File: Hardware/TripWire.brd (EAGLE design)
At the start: 27.3 x 45.2 mm, 40 parts, among them X1 GADGETEER-SOCKET

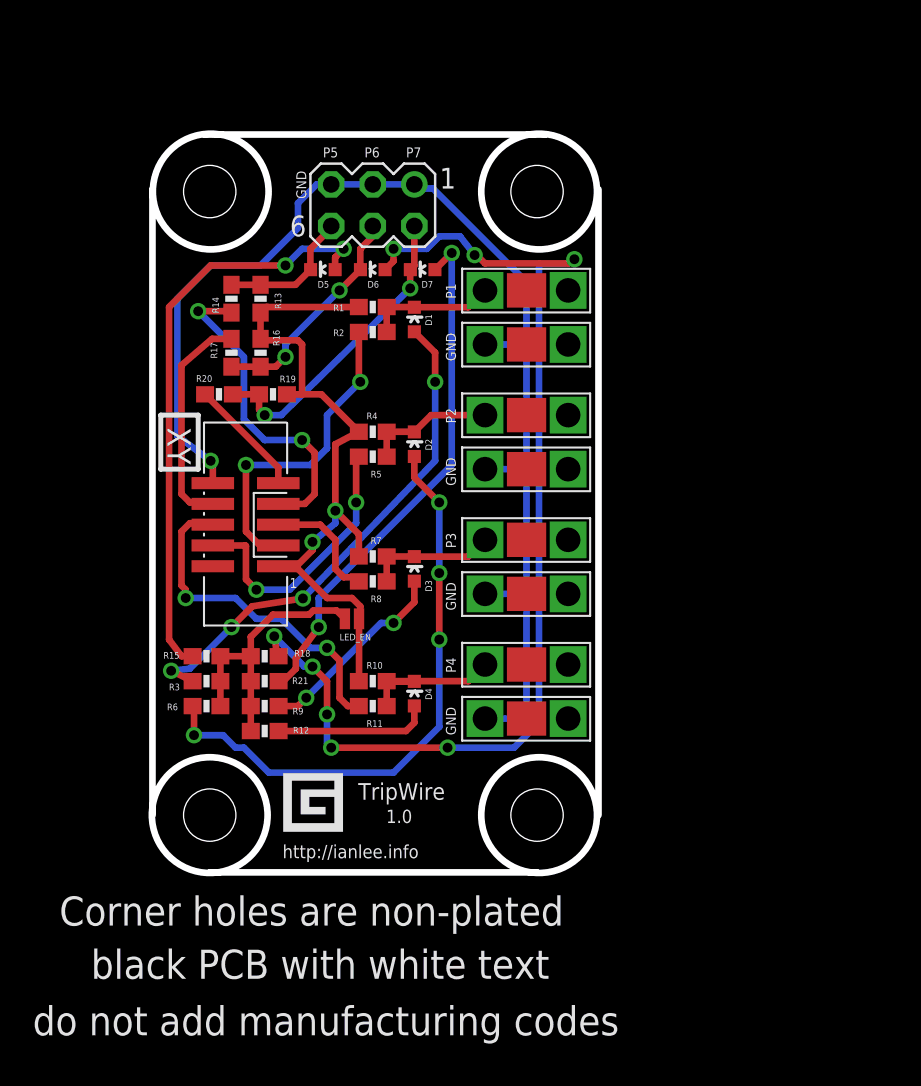
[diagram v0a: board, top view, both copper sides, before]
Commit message: Adjusted spade connector placement to give female connectors proper clearance.  Added trip wire logo to back.
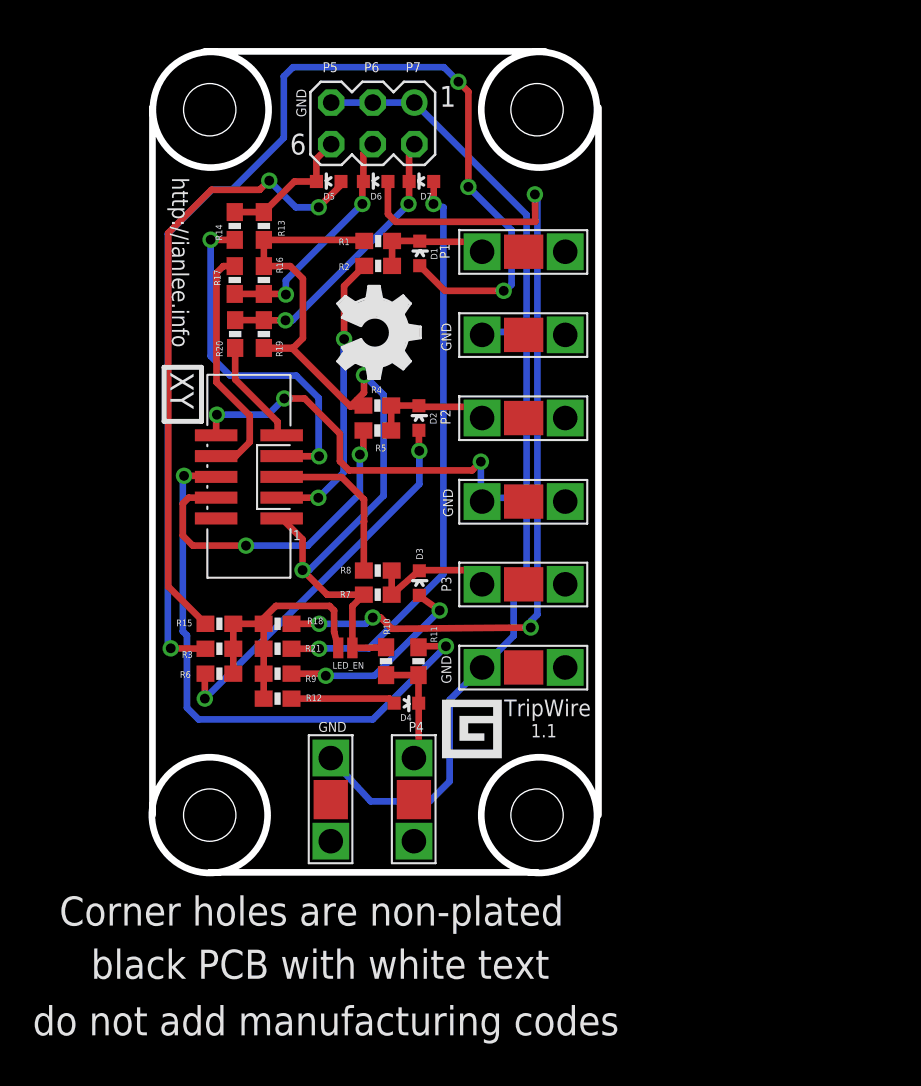
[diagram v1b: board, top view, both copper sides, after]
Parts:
- moved LOGO1 15.5 mm to (11.3, 35.8), flipped to the top, turned to 270 degrees
- moved U$8 8.48 mm to (10.9, 4.45), turned to 180 degrees
- moved U$7 8.45 mm to (16.0, 4.45), turned to 180 degrees
- moved U$6 6.65 mm to (22.7, 12.5)
- moved U$5 5.61 mm to (22.7, 17.6)
- moved U$1 5.44 mm to (22.7, 37.9)
- moved D5 5.40 mm to (10.8, 42.2)
- moved D6 5.39 mm to (13.6, 42.2)
- moved D7 5.39 mm to (16.4, 42.2)
- moved U$4 5.29 mm to (22.7, 22.7)
- moved SV1 5.00 mm to (13.5, 45.8)
- moved U$2 4.94 mm to (22.7, 32.8)
- moved U$3 4.91 mm to (22.7, 27.8)
- moved R13 4.45 mm to (6.81, 39.5)
- moved R14 4.45 mm to (5.03, 39.5)
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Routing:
- net N$1: track 31.2 -> 72.3 mm
- net PIN6: track 21.4 -> 36.0 mm
- net N$3: track 36.1 -> 23.4 mm, vias 4 -> 2
- net N$12: track 67.1 -> 54.6 mm, vias 8 -> 4
- net GND: track 76.8 -> 88.8 mm, vias 1 -> 3
- net 3V3: track 43.0 -> 54.9 mm
- net PIN4: track 16.9 -> 20.5 mm
- net N$10: track 32.0 -> 35.6 mm
- net N$7: track 9.53 -> 6.39 mm
- net PIN5: track 7.40 -> 9.96 mm
- net N$8: track 9.65 -> 7.18 mm
- net N$13: track 35.9 -> 38.1 mm
- net PIN3: track 19.8 -> 17.6 mm
- net PIN7: track 20.0 -> 22.1 mm
- net N$6: track 19.0 -> 17.4 mm
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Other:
- board size 27.3 x 45.2 mm -> 27.3 x 50.2 mm
- board text added: "1.1"
- board text added: "For driver & more info go to:"
- board text added: "XY"
- board text added: "http://ianlee.info/2013/01/tripwire-module.html"
- board text removed: "1.0"
- board text removed: "YX"

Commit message: Added pin breakout for non-Gadgeteer use.
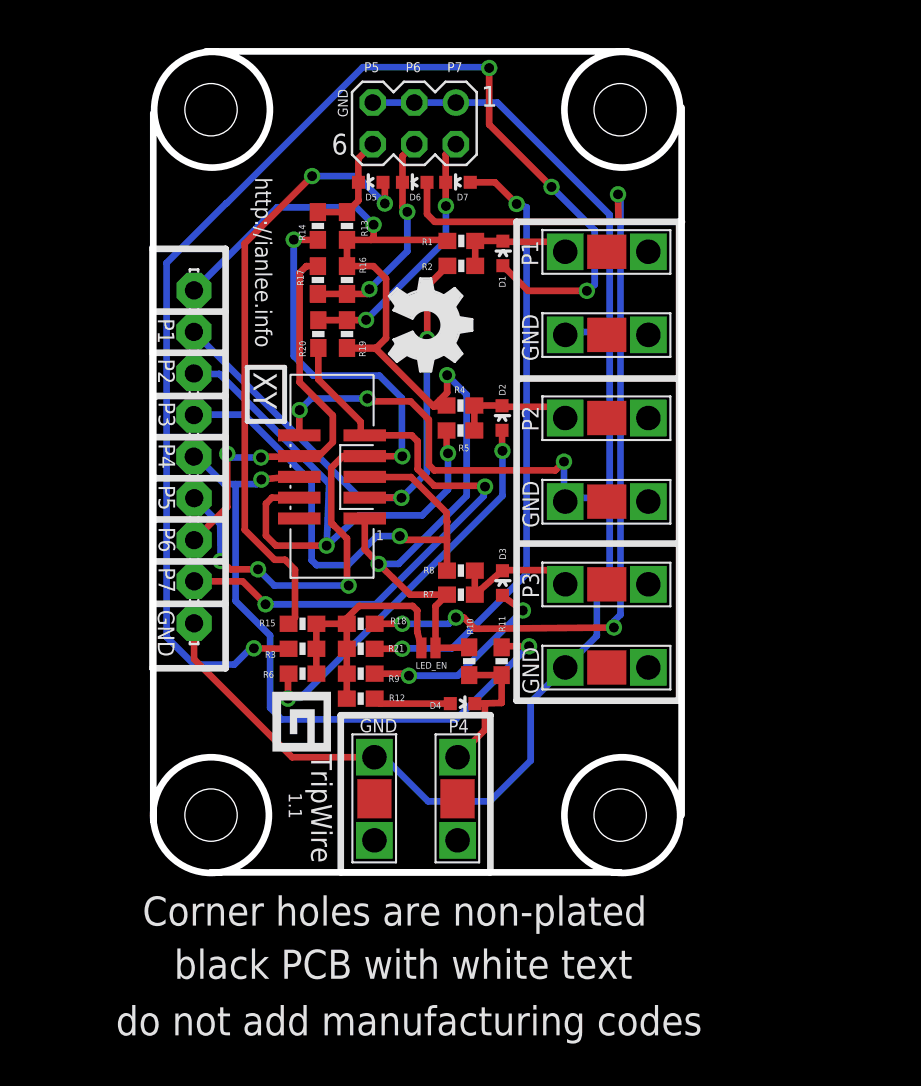
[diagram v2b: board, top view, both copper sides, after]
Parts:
- added 3V3, GND, P1, P2, P3, P4, P5, P6, P7: LSP11, solpad:LSP11
- moved D3 5.08 mm to (21.4, 17.7)
- moved R7 5.08 mm to (18.8, 17.0)
- moved R8 5.08 mm to (18.8, 18.4)
- moved R20 5.08 mm to (10.1, 32.9)
- moved LED_EN 5.08 mm to (16.9, 13.7)
- moved R1 5.08 mm to (18.9, 38.6)
- moved R10 5.08 mm to (19.4, 12.9)
- moved R12 5.08 mm to (12.7, 10.6)
- moved R13 5.08 mm to (11.9, 39.5)
- moved R16 5.08 mm to (11.9, 36.2)
- moved R18 5.08 mm to (12.7, 15.2)
- moved R19 5.08 mm to (11.9, 32.9)
- moved R2 5.08 mm to (18.9, 37.1)
- moved R21 5.08 mm to (12.7, 13.7)
- moved R4 5.08 mm to (18.8, 28.5)
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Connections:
- net 3V3: now also 3V3.MP
- net GND: now also GND.MP
- net PIN3: now also P1.MP
- net PIN4: now also P2.MP
- net PIN5: now also P3.MP
- net PIN6: now also P4.MP
- net PIN7: now also P5.MP
- net PIN8: now also P6.MP
- net PIN9: now also P7.MP
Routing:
- net PIN9: track 6.51 -> 37.8 mm, vias 0 -> 2
- net PIN7: track 22.1 -> 45.0 mm, vias 2 -> 5
- net PIN5: track 9.96 -> 32.4 mm, vias 0 -> 1
- net GND: track 88.8 -> 109.4 mm
- net PIN3: track 17.6 -> 34.5 mm
- net PIN4: track 20.5 -> 35.4 mm
- net 3V3: track 54.9 -> 69.7 mm, vias 2 -> 3
- net PIN8: track 14.9 -> 24.2 mm, vias 0 -> 2
- net N$1: track 72.3 -> 78.4 mm
- net PIN6: track 36.0 -> 41.6 mm
- net N$12: track 54.6 -> 57.3 mm
- net N$8: track 7.18 -> 9.31 mm
- net N$10: track 35.6 -> 37.7 mm
- net N$14: track 8.42 -> 6.58 mm
- net N$7: track 6.39 -> 4.75 mm
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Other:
- board size 27.3 x 50.2 mm -> 32.3 x 50.2 mm

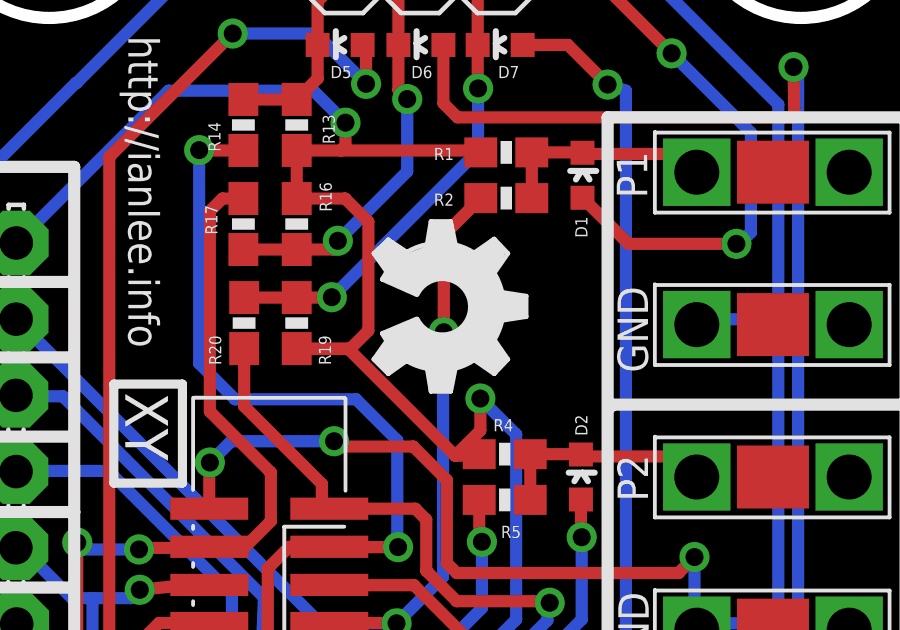
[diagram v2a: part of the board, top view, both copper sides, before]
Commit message: Updated OSHW logo.
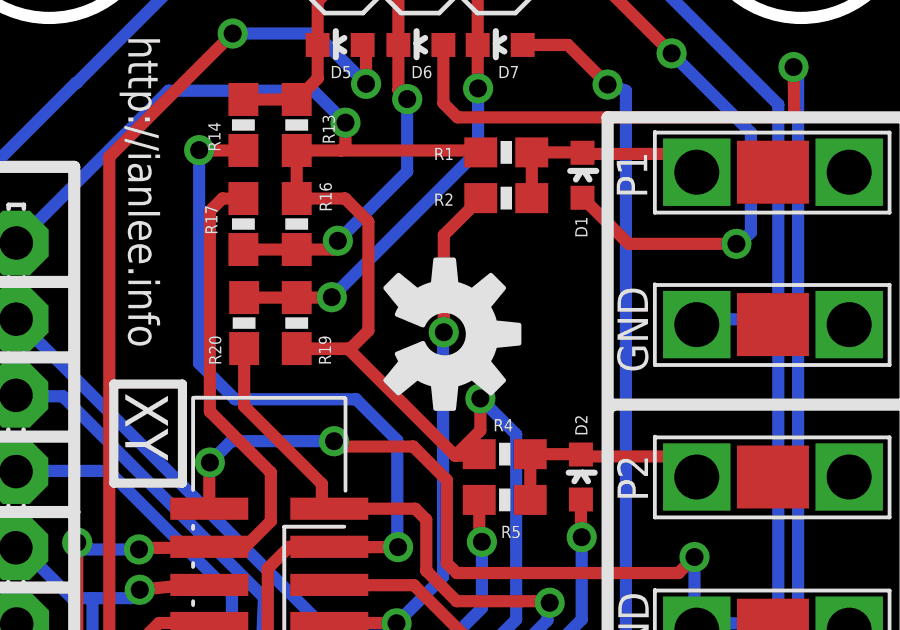
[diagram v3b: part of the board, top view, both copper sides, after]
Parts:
- LOGO1: value LOGO-OSHW-FILLX0200-NT -> OSHW-LOGOM; device Logo:OSHW_FILLX200_NOTEXT -> SparkFun-Aesthetics:OSHW-LOGO-M
- moved LOGO1 4.44 mm to (16.8, 32.5)
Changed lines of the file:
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@@
 <attribute name="VALUE" x="13.5128" y="31.8262" size="0.8128" layer="27" ratio="12" rot="R180"/>
 </element>
-<element name="LOGO1" library="Logo" package="OSHW_FILLX200_NOTEXT" value="LOGO-OSHW-FILLX0200-NT" x="14.4564" y="36.2826" rot="R270"/>
+<element name="LOGO1" library="SparkFun-Aesthetics" package="OSHW-LOGO-M" value="OSHW-LOGOM" x="16.8186" y="32.5234" rot="R270"/>
 <element name="U$1" library="SoftDust" package="SPADE-TERMINAL" value="SPADE-TERMINALPTH" x="27.7622" y="37.9222" smashed="yes" rot="R270"/>
 <element name="U$2" library="SoftDust" package="SPADE-TERMINAL" value="SPADE-TERMINALPTH" x="27.7622" y="32.8422" smashed="yes" rot="R270"/>

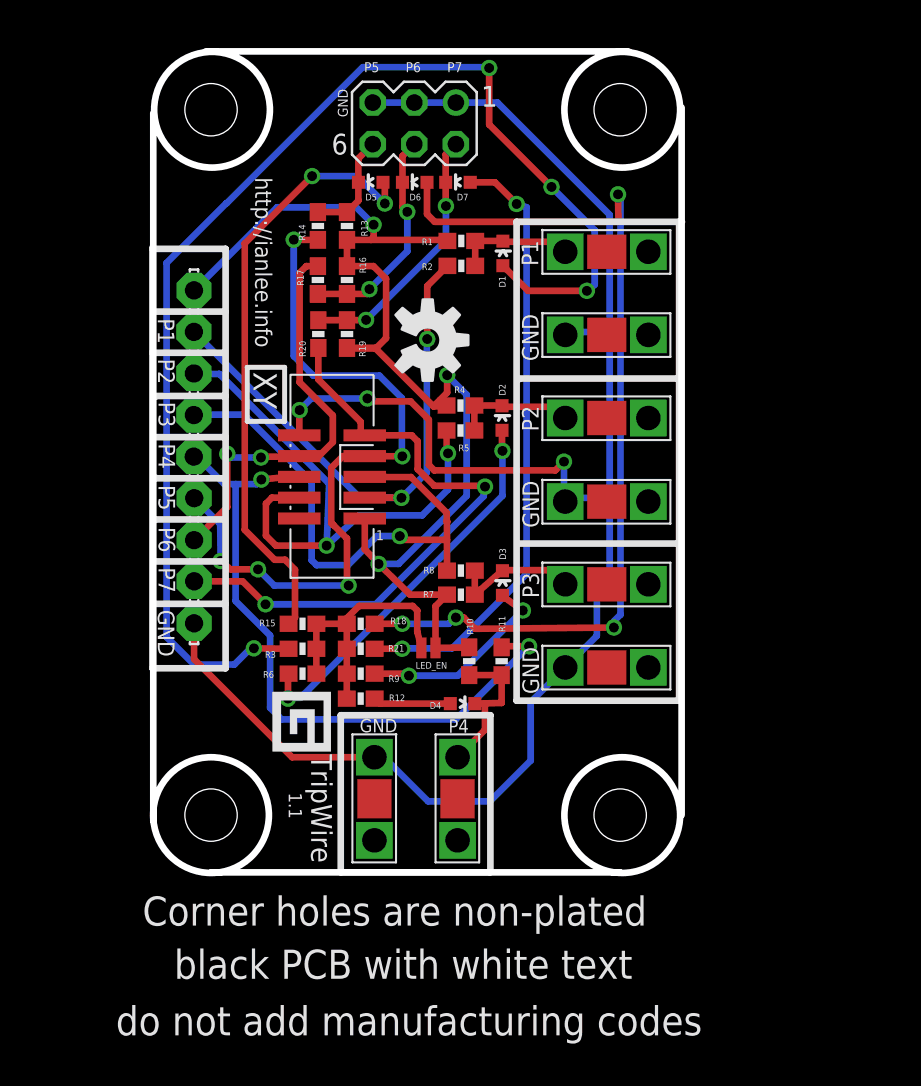
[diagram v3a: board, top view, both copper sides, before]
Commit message: Added pin protection diodes.
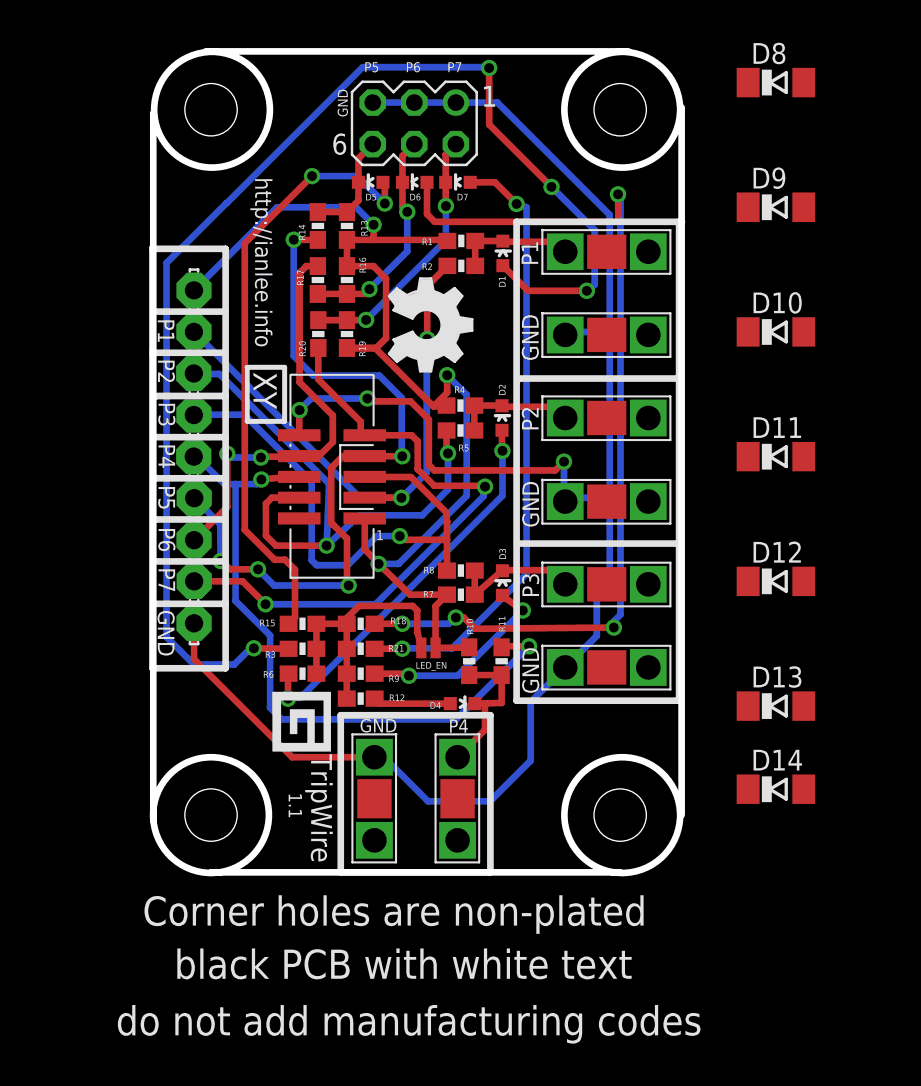
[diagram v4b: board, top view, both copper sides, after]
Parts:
- added D10, D11, D12, D13, D14, D8, D9: (no value), diode:SOD80C
- LOGO1: value OSHW-LOGOM -> LOGO-OSHW-FILLX0200-NT; device SparkFun-Aesthetics:OSHW-LOGO-M -> Logo:OSHW_FILLX200_NOTEXT
- moved LOGO1 4.44 mm to (14.5, 36.3)
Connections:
- new net N$15: D9.A
- new net N$16: D10.A
- net GND: now also D11.A, D12.A, D13.A, D14.A, D8.A
- net PIN3: now also D11.C
- net PIN4: now also D13.C
- net PIN5: now also D12.C
- net PIN6: now also D14.C
- net PIN7: now also D8.C
- net PIN8: now also D9.C
- net PIN9: now also D10.C
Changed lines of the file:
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@@
 <attribute name="VALUE" x="13.5128" y="31.8262" size="0.8128" layer="27" ratio="12" rot="R180"/>
 </element>
-<element name="LOGO1" library="SparkFun-Aesthetics" package="OSHW-LOGO-M" value="OSHW-LOGOM" x="16.8186" y="32.5234" rot="R270"/>
+<element name="LOGO1" library="Logo" package="OSHW_FILLX200_NOTEXT" value="LOGO-OSHW-FILLX0200-NT" x="14.4564" y="36.2826" rot="R270"/>
 <element name="U$1" library="SoftDust" package="SPADE-TERMINAL" value="SPADE-TERMINALPTH" x="27.7622" y="37.9222" smashed="yes" rot="R270"/>
 <element name="U$2" library="SoftDust" package="SPADE-TERMINAL" value="SPADE-TERMINALPTH" x="27.7622" y="32.8422" smashed="yes" rot="R270"/>
@@
 <attribute name="VALUE" x="2.295" y="17.7838" size="0.0254" layer="27" rot="R90"/>
 </element>
+<element name="D8" library="diode" package="SOD80C" value="" x="38.1" y="48.26"/>
+<element name="D9" library="diode" package="SOD80C" value="" x="38.1" y="40.64"/>
+<element name="D10" library="diode" package="SOD80C" value="" x="38.1" y="33.02"/>
+<element name="D11" library="diode" package="SOD80C" value="" x="38.1" y="25.4"/>
+<element name="D12" library="diode" package="SOD80C" value="" x="38.1" y="17.78"/>
+<element name="D13" library="diode" package="SOD80C" value="" x="38.1" y="10.16"/>
+<element name="D14" library="diode" package="SOD80C" value="" x="38.1" y="5.08"/>
 </elements>
 <signals>
@@
 <wire x1="15.7734" y1="28.7782" x2="13.3096" y2="28.7782" width="0.4064" layer="1"/>
 <wire x1="13.3096" y1="28.7782" x2="13.1318" y2="28.956" width="0.4064" layer="1"/>
-<wire x1="25.5778" y1="32.8422" x2="25.2222" y2="32.8422" width="0" layer="19" extent="16-16"/>
+<contactref element="D8" pad="A"/>
+<contactref element="D11" pad="A"/>
+<contactref element="D12" pad="A"/>
+<contactref element="D13" pad="A"/>
+<contactref element="D14" pad="A"/>
+<wire x1="39.8" y1="10.16" x2="39.8" y2="5.08" width="0" layer="19" extent="1-1"/>
+<wire x1="39.8" y1="17.78" x2="39.8" y2="10.16" width="0" layer="19" extent="1-1"/>
+<wire x1="39.8" y1="25.4" x2="39.8" y2="17.78" width="0" layer="19" extent="1-1"/>
+<wire x1="39.8" y1="48.26" x2="39.8" y2="25.4" width="0" layer="19" extent="1-1"/>
+<wire x1="8.5344" y1="7.0358" x2="39.8" y2="48.26" width="0" layer="19" extent="1-1"/>
+<wire x1="25.2222" y1="32.8422" x2="25.5778" y2="32.8422" width="0" layer="19" extent="16-16"/>
 </signal>
 <signal name="+5V" class="1">
@@
 <wire x1="2.535" y1="33.0238" x2="12.6734" y2="22.8854" width="0.4064" layer="16"/>
 <wire x1="12.6734" y1="22.8854" x2="15.2146" y2="22.8854" width="0.4064" layer="16"/>
+<contactref element="D11" pad="C"/>
+<wire x1="12.6734" y1="22.8854" x2="36.4" y2="25.4" width="0" layer="19" extent="1-16"/>
 </signal>
 <signal name="PIN4">
@@
 <wire x1="7.5438" y1="19.9644" x2="10.6426" y2="19.9644" width="0.4064" layer="1"/>
 <via x="10.6426" y="19.9644" extent="1-16" drill="0.6" shape="square"/>
-<wire x1="17.7546" y1="25.5016" x2="18.0594" y2="25.6032" width="0" layer="19" extent="1-16"/>
 <via x="18.0594" y="25.6032" extent="1-16" drill="0.6" shape="square"/>
 <wire x1="18.0594" y1="25.6032" x2="17.9714" y2="25.7438" width="0.4064" layer="1"/>
@@
 <wire x1="16.4846" y1="21.8186" x2="18.0594" y2="23.3934" width="0.4064" layer="16"/>
 <wire x1="18.0594" y1="23.3934" x2="18.0594" y2="25.6032" width="0.4064" layer="16"/>
+<contactref element="D13" pad="C"/>
+<wire x1="7.5438" y1="19.9644" x2="36.4" y2="10.16" width="0" layer="19" extent="1-1"/>
 </signal>
 <signal name="PIN5">
@@
 <wire x1="17.9832" y1="21.971" x2="17.9832" y2="21.4612" width="0.4064" layer="1"/>
 <wire x1="17.9832" y1="21.4612" x2="18.0086" y2="21.4358" width="0.4064" layer="1"/>
+<contactref element="D12" pad="C"/>
+<wire x1="10.033" y1="18.7706" x2="36.4" y2="17.78" width="0" layer="19" extent="1-16"/>
 </signal>
 <signal name="PIN7">
@@
 <wire x1="10.922" y1="24.7142" x2="11.644" y2="25.4362" width="0.4064" layer="1"/>
 <wire x1="11.644" y1="25.4362" x2="12.9728" y2="25.4362" width="0.4064" layer="1"/>
+<contactref element="D8" pad="C"/>
+<wire x1="36.4" y1="48.26" x2="7.4422" y2="17.526" width="0" layer="19" extent="1-16"/>
 </signal>
 <signal name="PIN9">
@@
 <wire x1="17.2212" y1="23.622" x2="20.2692" y2="23.622" width="0.4064" layer="1"/>
 <wire x1="20.2692" y1="23.622" x2="20.32" y2="23.5712" width="0.4064" layer="1"/>
+<contactref element="D10" pad="C"/>
+<wire x1="6.9088" y1="16.383" x2="36.4" y2="33.02" width="0" layer="19" extent="1-1"/>
 </signal>
 <signal name="PIN6">
@@
 <wire x1="7.1882" y1="14.478" x2="5.08" y2="16.5862" width="0.4064" layer="16"/>
 <wire x1="5.08" y1="16.5862" x2="5.08" y2="23.7236" width="0.4064" layer="16"/>
+<contactref element="D14" pad="C"/>
+<wire x1="7.8994" y1="9.3472" x2="36.4" y2="5.08" width="0" layer="19" extent="1-16"/>
 </signal>
 <signal name="PIN8">
@@
 <wire x1="2.5464" y1="20.2984" x2="4.572" y2="22.324" width="0.4064" layer="1"/>
 <wire x1="4.572" y1="22.324" x2="4.572" y2="25.5778" width="0.4064" layer="1"/>
+<contactref element="D9" pad="C"/>
 <wire x1="7.62" y1="25.4" x2="8.9728" y2="25.4362" width="0" layer="19" extent="1-1"/>
+<wire x1="36.4" y1="40.64" x2="2.5464" y2="20.2984" width="0" layer="19" extent="1-1"/>
 </signal>
 <signal name="N$13">
@@
 <wire x1="17.919" y1="43.874" x2="18.542" y2="44.497" width="0.4064" layer="1"/>
 </signal>
+<signal name="N$15">
+<contactref element="D9" pad="A"/>
+</signal>
+<signal name="N$16">
+<contactref element="D10" pad="A"/>
+</signal>
 </signals>
